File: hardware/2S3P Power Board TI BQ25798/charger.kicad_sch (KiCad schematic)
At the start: 58 parts, among them J701 Thermistor Override, J702 PEC02SAAN, J703 Solar Input, U701 BQ25798RQMR

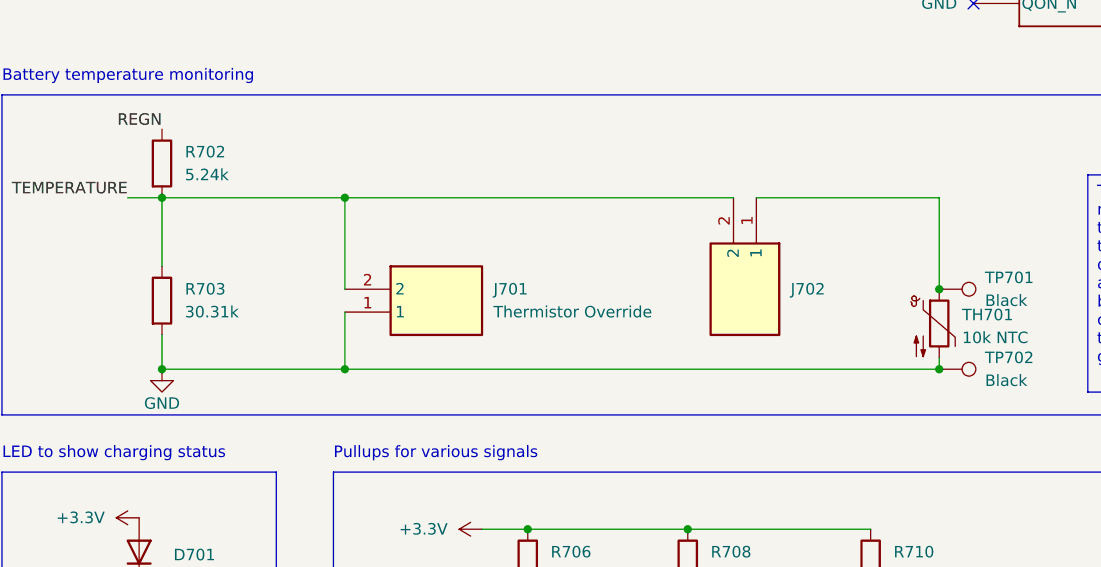
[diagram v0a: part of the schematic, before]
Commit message: Filling in specific MPNs and verifying active status on a few more parts
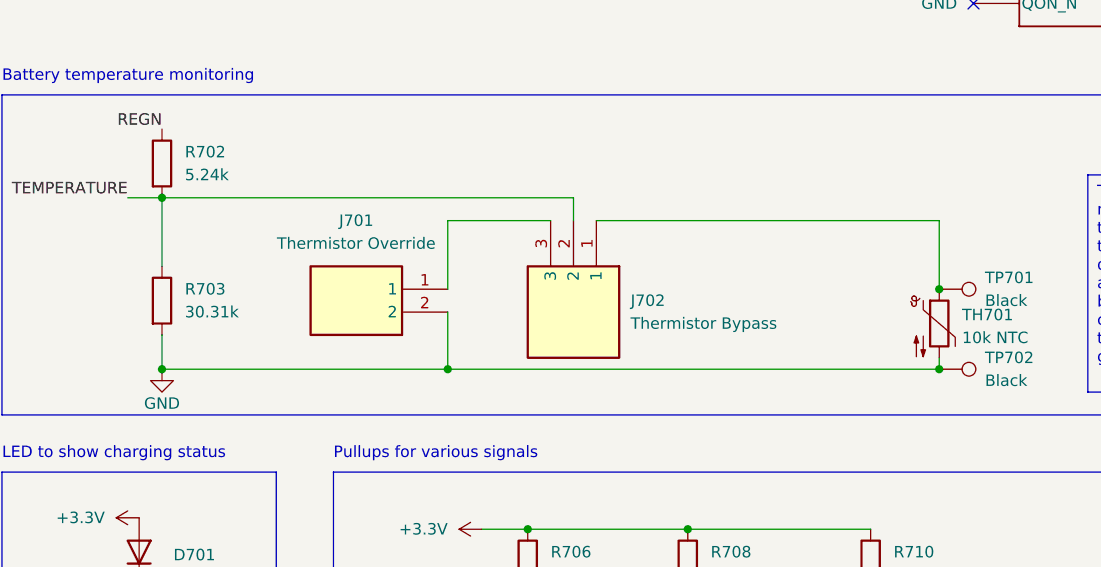
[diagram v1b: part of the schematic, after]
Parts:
- removed J702: PEC02SAAN, footprints:HDRV2W64P0X254_1X2_508X254X838P, symbol Sullins PEC02SAAN:PEC02SAAN
- added J702: Thermistor Bypass, footprints:HDRV3W64P0X254_1X3_762X254X838P, symbol Sullins PEC03SAAN:PEC03SAAN
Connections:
- net GND: now also J701.2; no longer J701.1
- net TEMPERATURE: now also J702.2; no longer J701.2
- net at TH701.1, TP701.1: now also J702.1
- new net: J701.1, J702.3
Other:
- moved on the sheet: J701

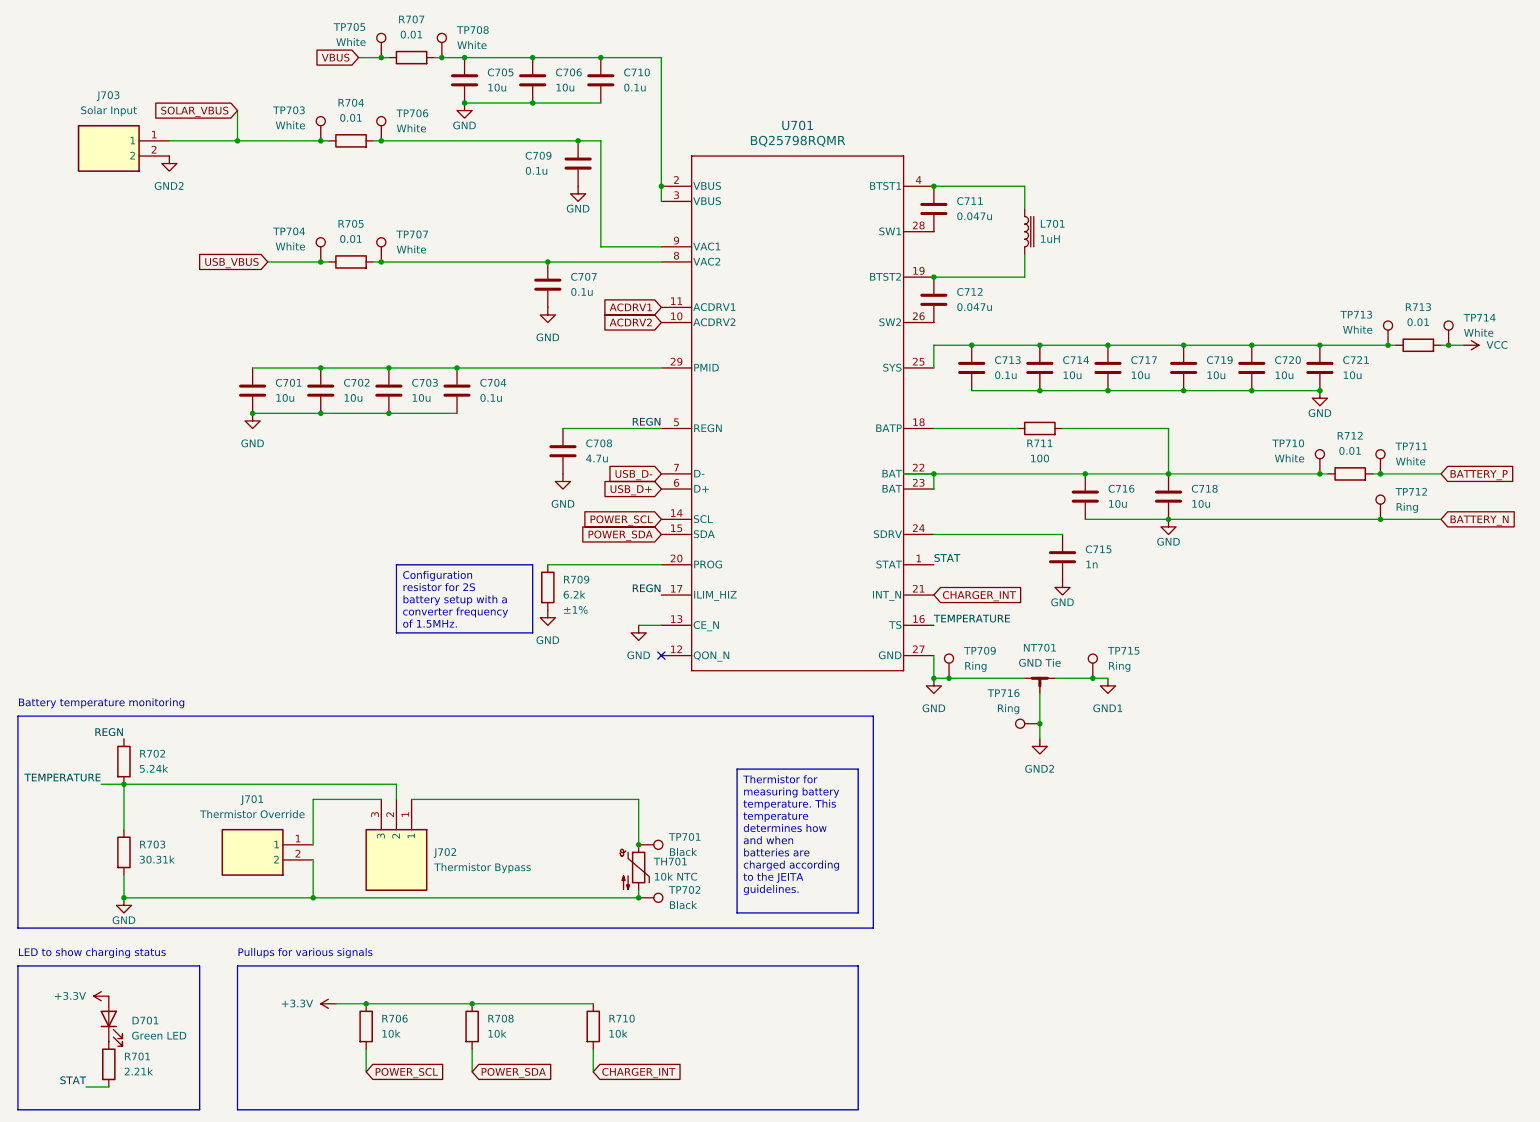
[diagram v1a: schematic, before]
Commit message: Reordered the sheets
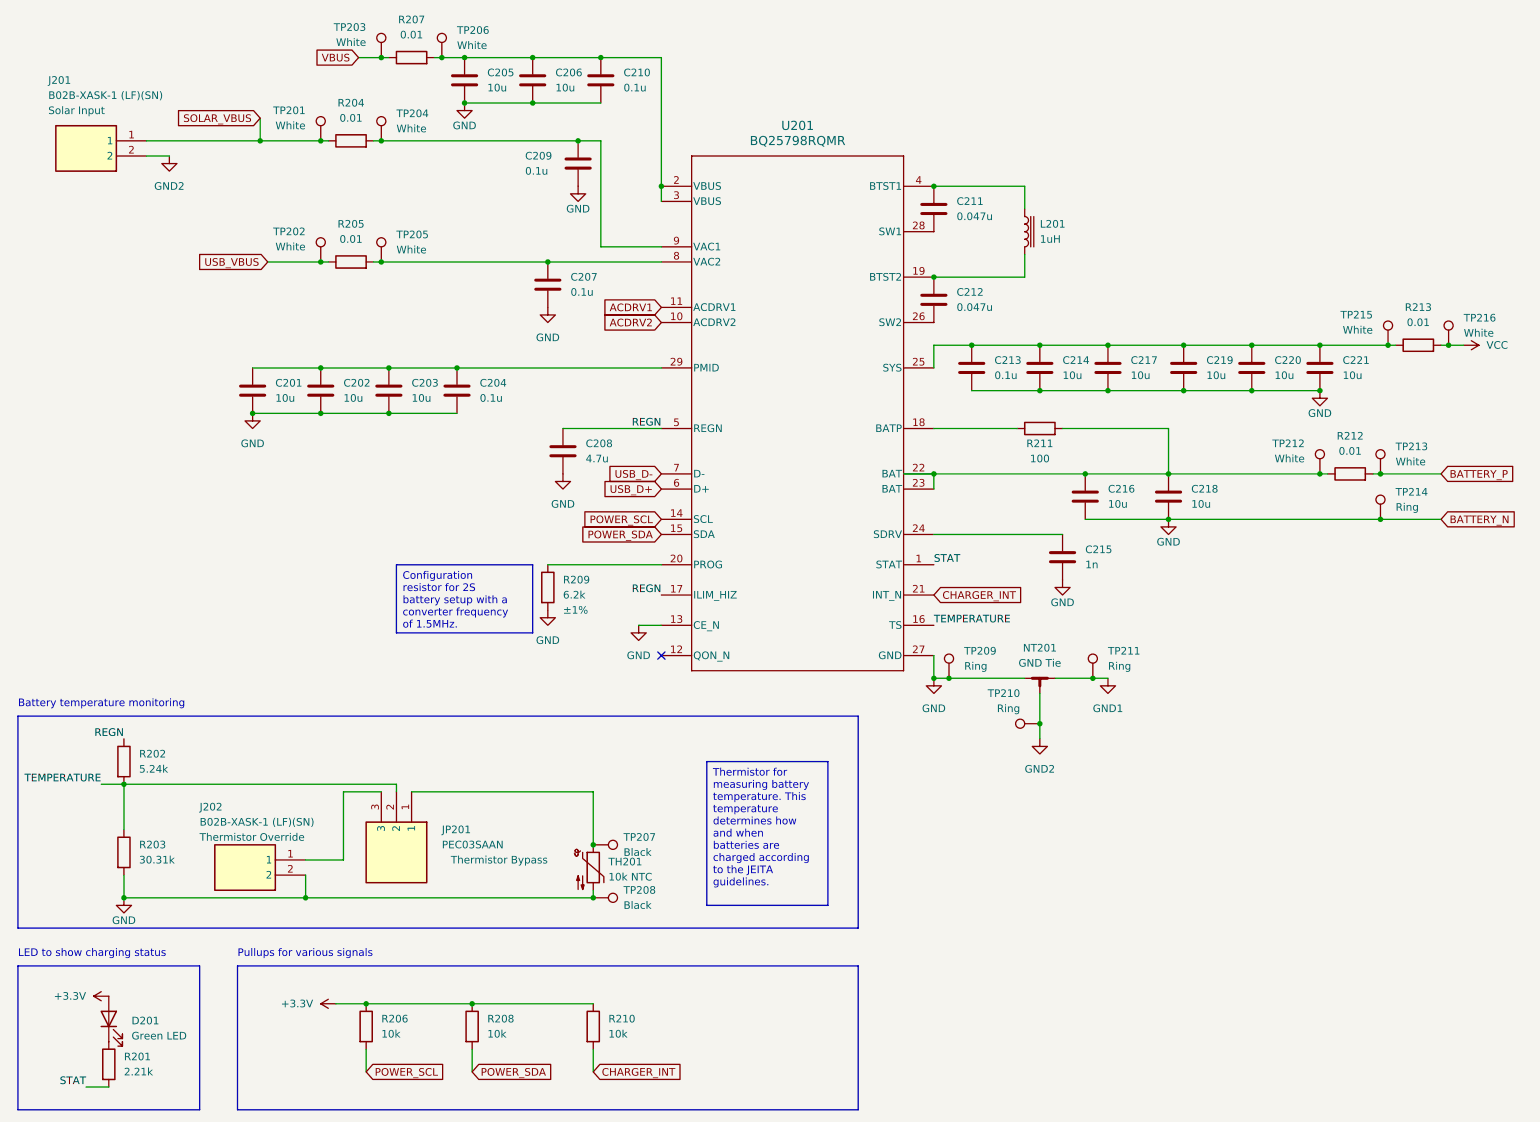
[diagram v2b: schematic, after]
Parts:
- J201: renamed from J703; value Solar Input -> B02B-XASK-1 (LF)(SN); Purpose (none) -> Solar Input
- J202: renamed from J701; value Thermistor Override -> B02B-XASK-1 (LF)(SN); Purpose (none) -> Thermistor Override
- JP201: renamed from J702; value Thermistor Bypass -> PEC03SAAN; Purpose (none) -> Thermistor Bypass
- renumbered C701 to C201, C702 to C202, C703 to C203, C704 to C204, C705 to C205, C706 to C206, C707 to C207, C708 to C208, C709 to C209, C710 to C210, C711 to C211, C712 to C212, C713 to C213, C714 to C214, C715 to C215, C716 to C216, C717 to C217, C718 to C218, C719 to C219, C720 to C220, C721 to C221, D701 to D201, L701 to L201, NT701 to NT201, R701 to R201, R702 to R202, R703 to R203, R704 to R204, R705 to R205, R706 to R206, R707 to R207, R708 to R208, R709 to R209, R710 to R210, R711 to R211, R712 to R212, R713 to R213, TH701 to TH201, TP703 to TP201, TP704 to TP202, TP705 to TP203, TP706 to TP204, TP707 to TP205, TP708 to TP206, TP701 to TP207, TP702 to TP208, TP709 to TP209, TP716 to TP210, TP715 to TP211, TP710 to TP212, TP711 to TP213, TP712 to TP214, TP713 to TP215, TP714 to TP216, U701 to U201
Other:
- moved on the sheet: J201, J202, JP201, TH201, TP207, TP208

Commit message: Verified several more parts
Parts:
- J201, J202: MPN (none) -> C263753; Manufacturer (none) -> JST; Manufacturer Part Number (none) -> B02B-XASK-1(LF)(SN)
- JP201: value PEC03SAAN -> 3P Header; footprint footprints:HDRV3W64P0X254_1X3_762X254X838P -> footprints:HDRV3W64P0X254_1X3_762X254X869P; symbol Sullins PEC03SAAN:PEC03SAAN -> Würth 61300311121:61300311121; Active (none) -> Y; Height 8.38 -> 8.69; MPN (none) -> C2915006; Manufacturer (none) -> Wurth Elektronik; Manufacturer Part Number (none) -> 61300311121; Manufacturer_Name Sullins -> Wurth Elektronik; Manufacturer_Part_Number PEC03SAAN -> 61300311121; Mouser Part Number (none) -> 710-61300311121; Mouser Price/Stock (none) -> https://www.mouser.co.uk/ProductDetail/Wurth-Elektronik/613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
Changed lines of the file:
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@@
       (effects (font (size 1.27 1.27)) (justify right))
+    )
+    (property "MPN" "C263753" (at 60.96 163.83 0)
+      (effects (font (size 1.27 1.27)) hide)
+    )
+    (property "Manufacturer" "JST" (at 60.96 163.83 0)
+      (effects (font (size 1.27 1.27)) hide)
+    )
+    (property "Manufacturer Part Number" "B02B-XASK-1(LF)(SN)" (at 60.96 163.83 0)
+      (effects (font (size 1.27 1.27)) hide)
     )
     (pin "2")
@@
     )
   )
-  (symbol (lib_id "Sullins PEC03SAAN:PEC03SAAN") (at 78.74 149.86 270) (unit 1)
+  (symbol (lib_id "Würth 61300311121:61300311121") (at 78.74 149.86 270) (unit 1)
     (in_bom yes) (on_board yes) (dnp no)
     (property "Reference" "JP201" (at 83.82 156.21 90)
       (effects (font (size 1.27 1.27)) (justify left))
     )
-    (property "Value" "PEC03SAAN" (at 83.82 158.75 90)
-      (effects (font (size 1.27 1.27)) (justify left))
-    )
-    (property "Footprint" "footprints:HDRV3W64P0X254_1X3_762X254X838P" (at -16.18 166.37 0)
-      (effects (font (size 1.27 1.27)) (justify left top) hide)
-    )
-    (property "Datasheet" "" (at -116.18 166.37 0)
-      (effects (font (size 1.27 1.27)) (justify left top) hide)
-    )
-    (property "Height" "8.38" (at -316.18 166.37 0)
-      (effects (font (size 1.27 1.27)) (justify left top) hide)
-    )
-    (property "Manufacturer_Name" "Sullins" (at -416.18 166.37 0)
-      (effects (font (size 1.27 1.27)) (justify left top) hide)
-    )
-    (property "Manufacturer_Part_Number" "PEC03SAAN" (at -516.18 166.37 0)
-      (effects (font (size 1.27 1.27)) (justify left top) hide)
-    )
-    (property "Mouser Part Number" "" (at -616.18 166.37 0)
-      (effects (font (size 1.27 1.27)) (justify left top) hide)
-    )
-    (property "Mouser Price/Stock" "" (at -716.18 166.37 0)
+    (property "Value" "3P Header" (at 83.82 158.75 90)
+      (effects (font (size 1.27 1.27)) (justify left))
+    )
+    (property "Footprint" "footprints:HDRV3W64P0X254_1X3_762X254X869P" (at -16.18 166.37 0)
+      (effects (font (size 1.27 1.27)) (justify left top) hide)
+    )
+    (property "Datasheet" "http://katalog.we-online.de/em/datasheet/6130xx11121.pdf" (at -116.18 166.37 0)
+      (effects (font (size 1.27 1.27)) (justify left top) hide)
+    )
+    (property "Height" "8.69" (at -316.18 166.37 0)
+      (effects (font (size 1.27 1.27)) (justify left top) hide)
+    )
+    (property "Manufacturer_Name" "Wurth Elektronik" (at -416.18 166.37 0)
+      (effects (font (size 1.27 1.27)) (justify left top) hide)
+    )
+    (property "Manufacturer_Part_Number" "61300311121" (at -516.18 166.37 0)
+      (effects (font (size 1.27 1.27)) (justify left top) hide)
+    )
+    (property "Mouser Part Number" "710-61300311121" (at -616.18 166.37 0)
+      (effects (font (size 1.27 1.27)) (justify left top) hide)
+    )
+    (property "Mouser Price/Stock" "https://www.mouser.co.uk/ProductDetail/Wurth-Elektronik/61300311121?qs=PhR8RmCirEYxRWFJzNKsUw%3D%3D" (at -716.18 166.37 0)
       (effects (font (size 1.27 1.27)) (justify left top) hide)
     )
@@
     (property "Purpose" "Thermistor Bypass" (at 101.6 161.29 90)
       (effects (font (size 1.27 1.27)) (justify right))
+    )
+    (property "MPN" "C2915006" (at 78.74 149.86 0)
+      (effects (font (size 1.27 1.27)) hide)
+    )
+    (property "Manufacturer" "Wurth Elektronik" (at 78.74 149.86 0)
+      (effects (font (size 1.27 1.27)) hide)
+    )
+    (property "Manufacturer Part Number" "61300311121" (at 78.74 149.86 0)
+      (effects (font (size 1.27 1.27)) hide)
+    )
+    (property "Active" "Y" (at 78.74 149.86 0)
+      (effects (font (size 1.27 1.27)) hide)
     )
     (pin "3")
@@
       (effects (font (size 1.27 1.27)) (justify right))
     )
-    (pin "2")
+    (property "MPN" "C263753" (at 34.29 43.18 0)
+      (effects (font (size 1.27 1.27)) hide)
+    )
+    (property "Manufacturer" "JST" (at 34.29 43.18 0)
+      (effects (font (size 1.27 1.27)) hide)
+    )
+    (property "Manufacturer Part Number" "B02B-XASK-1(LF)(SN)" (at 34.29 43.18 0)
+      (effects (font (size 1.27 1.27)) hide)
+    )
+    (pin "2")

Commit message: Verified remaining components
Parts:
- J201, J202, R204, R205, R206, R207, R208, R210, R211, R212, R213: Active (none) -> Y
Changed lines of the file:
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@@
       (effects (font (size 1.27 1.27)) hide)
     )
-    (property "Active" "" (at 71.12 189.23 0)
+    (property "Active" "Y" (at 71.12 189.23 0)
       (effects (font (size 1.27 1.27)) hide)
     )
@@
       (effects (font (size 1.27 1.27)) hide)
     )
+    (property "Active" "Y" (at 68.58 60.96 0)
+      (effects (font (size 1.27 1.27)) hide)
+    )
     (pin "1")
     (pin "2")
@@
       (effects (font (size 1.27 1.27)) hide)
     )
-    (property "Active" "" (at 88.9 189.23 0)
+    (property "Active" "Y" (at 88.9 189.23 0)
       (effects (font (size 1.27 1.27)) hide)
     )
@@
       (effects (font (size 1.27 1.27)) hide)
     )
+    (property "Active" "Y" (at 60.96 163.83 0)
+      (effects (font (size 1.27 1.27)) hide)
+    )
     (pin "2")
     (pin "1")
@@
       (effects (font (size 1.27 1.27)) hide)
     )
-    (property "Active" "" (at 184.15 88.9 0)
+    (property "Active" "Y" (at 184.15 88.9 0)
       (effects (font (size 1.27 1.27)) hide)
     )
@@
     )
     (property "Purpose" "" (at 68.58 40.64 0)
+      (effects (font (size 1.27 1.27)) hide)
+    )
+    (property "Active" "Y" (at 68.58 40.64 0)
       (effects (font (size 1.27 1.27)) hide)
     )
@@
       (effects (font (size 1.27 1.27)) hide)
     )
+    (property "Active" "Y" (at 34.29 43.18 0)
+      (effects (font (size 1.27 1.27)) hide)
+    )
     (pin "2")
     (pin "1")
@@
       (effects (font (size 1.27 1.27)) hide)
     )
+    (property "Active" "Y" (at 247.65 74.93 0)
+      (effects (font (size 1.27 1.27)) hide)
+    )
     (pin "1")
     (pin "2")
@@
     )
     (property "Purpose" "" (at 236.22 96.52 0)
+      (effects (font (size 1.27 1.27)) hide)
+    )
+    (property "Active" "Y" (at 236.22 96.52 0)
       (effects (font (size 1.27 1.27)) hide)
     )
@@
       (effects (font (size 1.27 1.27)) hide)
     )
+    (property "Active" "Y" (at 78.74 26.67 0)
+      (effects (font (size 1.27 1.27)) hide)
+    )
     (pin "1")
     (pin "2")
@@
       (effects (font (size 1.27 1.27)) hide)
     )
-    (property "Active" "" (at 109.22 189.23 0)
-      (effects (font (size 1.27 1.27)) hide)
-    )
+    (property "Active" "Y" (at 109.22 189.23 0)
+      (effects (font (size 1.27 1.27)) hide)
+    )
